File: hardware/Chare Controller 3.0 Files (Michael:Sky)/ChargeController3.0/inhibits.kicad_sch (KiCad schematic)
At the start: 16 parts, among them J19 SYS-1x2, J2 SP_01x02_Pin, J5 BATT_01x02_Pin, Q1 SI2318CDS-T1-GE3, Q10 SI2318CDS-T1-GE3, Q11 SI2318CDS-T1-GE3, Q12 SI2318CDS-T1-GE3, Q2 SI2318CDS-T1-GE3, Q3 SI2318CDS-T1-GE3, Q4 SI2318CDS-T1-GE3, Q9 SI2318CDS-T1-GE3, SW1 100SP1T1B1M1QEH

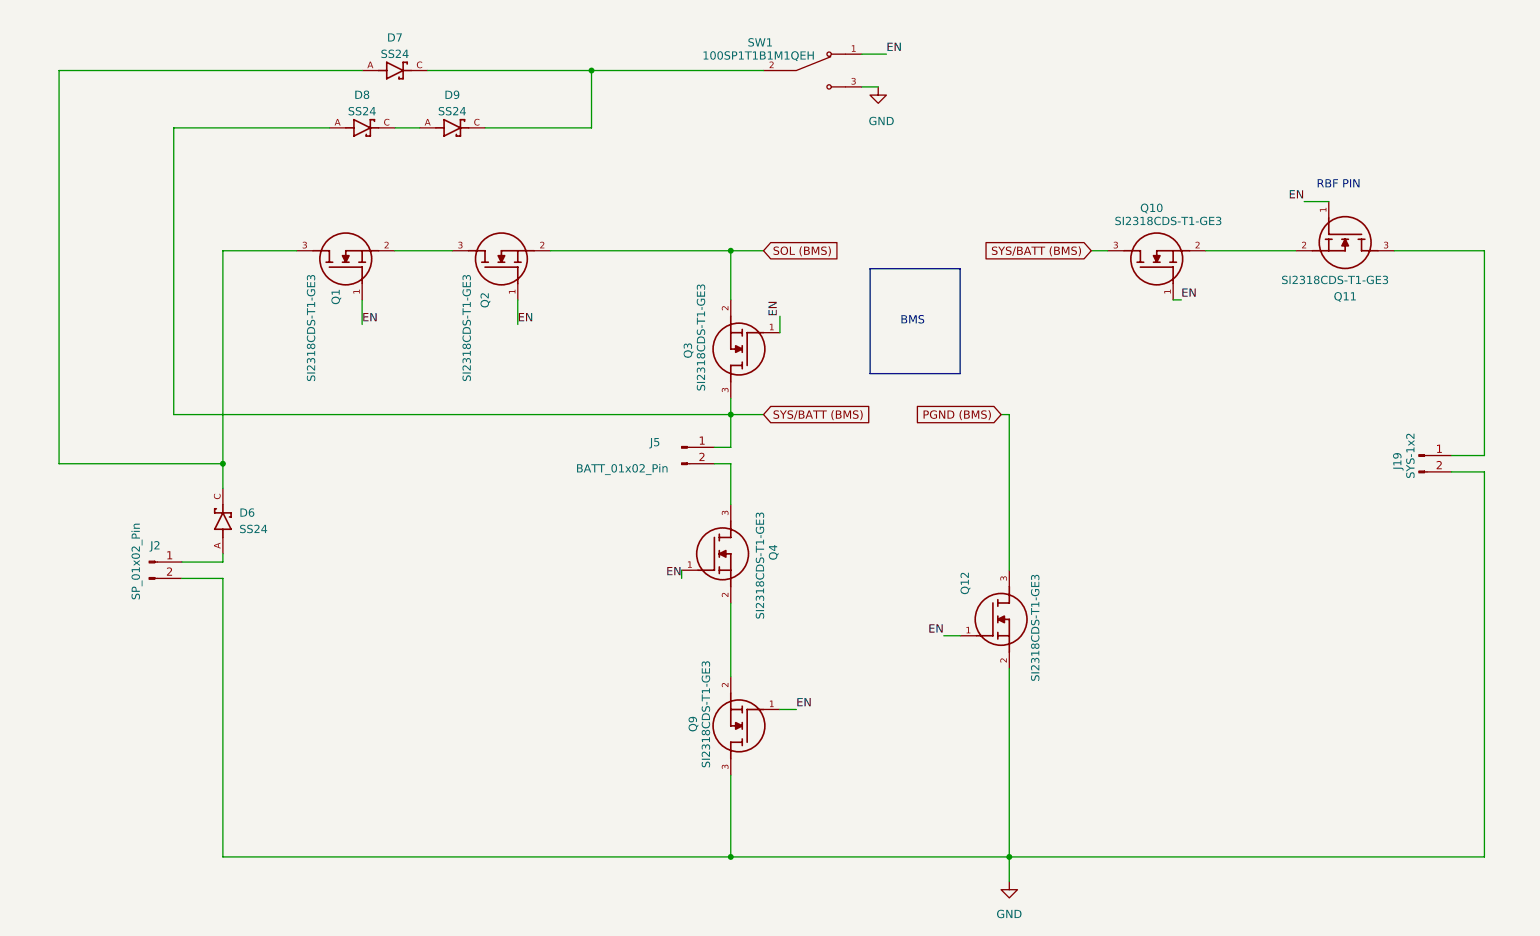
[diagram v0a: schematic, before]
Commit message: Charge Controller 3.0
Next Prototype formatting (Schematic Format Done)
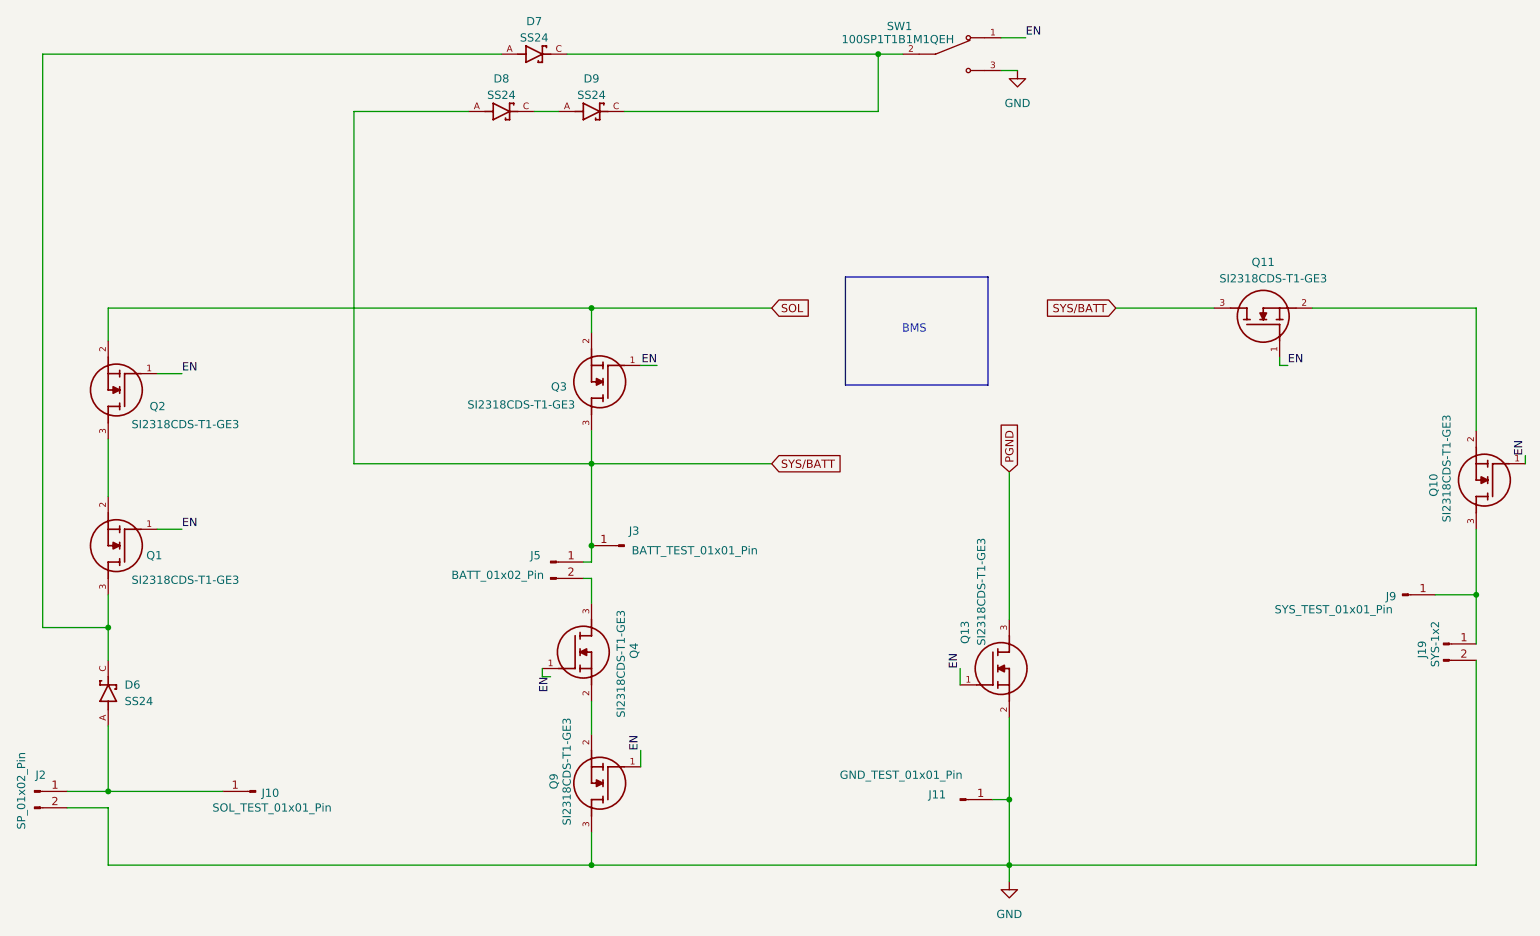
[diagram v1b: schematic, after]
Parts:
- removed Q12: SI2318CDS-T1-GE3, bmsfootprints:SI2318CDS-T1-GE3, symbol SI2318CDS-T1-GE3:SI2318CDS-T1-GE3
- added J10: SOL_TEST_01x01_Pin, Connector_PinHeader_2.54mm:PinHeader_1x01_P2.54mm_Vertical, symbol Connector:Conn_01x01_Pin
- added J11: GND_TEST_01x01_Pin, Connector_PinHeader_2.54mm:PinHeader_1x01_P2.54mm_Vertical, symbol Connector:Conn_01x01_Pin
- added J3: BATT_TEST_01x01_Pin, Connector_PinHeader_2.54mm:PinHeader_1x01_P2.54mm_Vertical, symbol Connector:Conn_01x01_Pin
- added J9: SYS_TEST_01x01_Pin, Connector_PinHeader_2.54mm:PinHeader_1x01_P2.54mm_Vertical, symbol Connector:Conn_01x01_Pin
- added Q13: SI2318CDS-T1-GE3, bmsfootprints:SI2318CDS-T1-GE3, symbol SI2318CDS-T1-GE3:SI2318CDS-T1-GE3
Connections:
- net EN: now also Q13.1
- net GND: now also J11.1 (Pin_1), Q13.2
- net at J19.1 (Pin_1): now also Q10.3, J9.1 (Pin_1); no longer Q11.3
- net at D6.A, J2.1 (Pin_1): now also J10.1 (Pin_1)
- net SOL (BMS) renamed SOL
- net SYS/BATT (BMS) renamed SYS/BATT
- net SYS/BATT: now also Q11.3, J3.1 (Pin_1); no longer Q10.3
- new net PGND: Q13.3
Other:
- note removed: "RBF PIN"
- moved on the sheet: D6, D7, D8, D9, J19, J2, J5, Q1, Q10, Q11, Q2, Q3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
